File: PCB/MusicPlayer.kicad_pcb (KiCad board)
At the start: 4 copper layers, 96 x 96 mm, 79 parts, among them J1 3.7v LiPo, J2 USB_C_Receptacle_USB2.0_16P, J3 SSD1306D, J4 Conn_ST_STDC14, Q1 MMBT2907ALT1HTSA1, Q2 NMOS, SW1 ON_OFF, SW2 RESET, SW3 PLAY_PAUSE, SW4 NEXT, SW5 PREV, SW6 RotaryEncoder, U1 TPS61090, U2 LD1117S33TR_SOT223, U3 MCP73831T-2ACI/OT, U4 STM32G031K8Ux, U5 Music Maker FeatherWing, U6 MAX17048G, U7 USBLC6-2P6, U8 CH340C

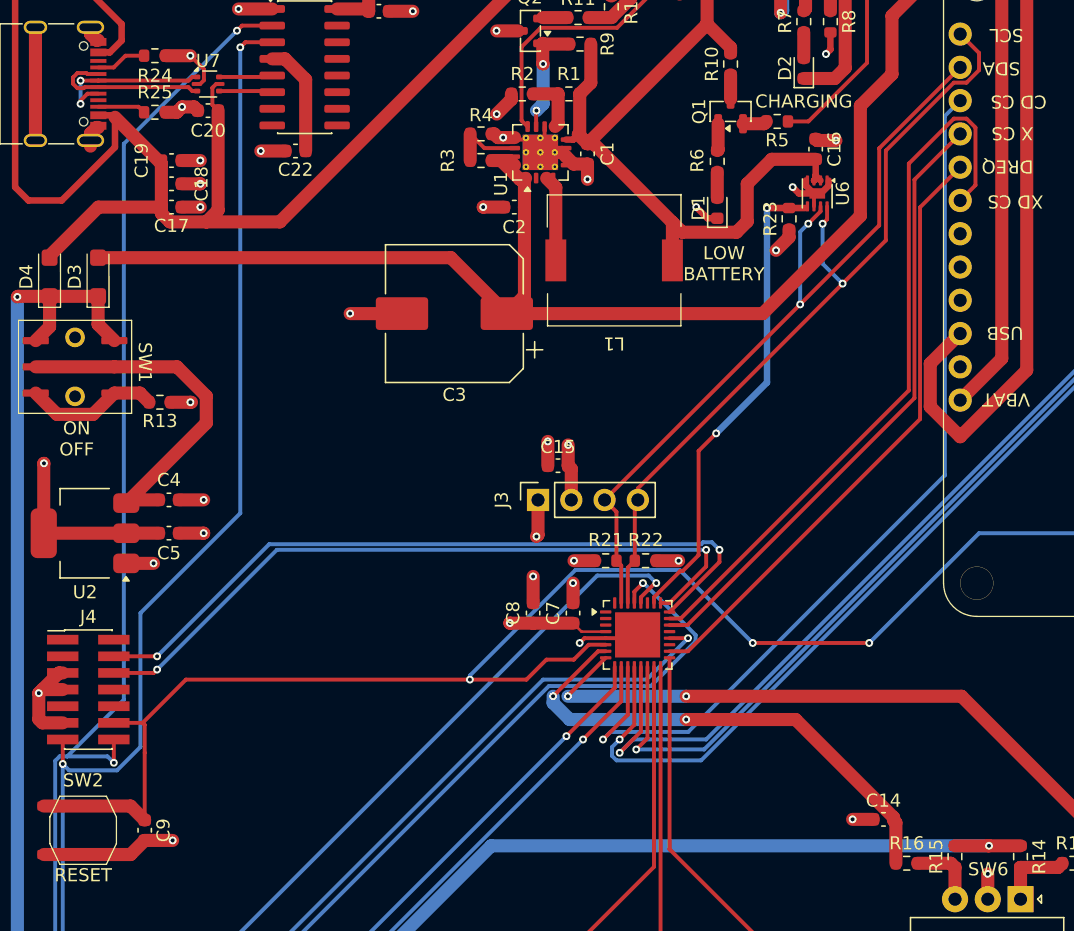
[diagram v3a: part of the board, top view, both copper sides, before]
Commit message: Finished making a PCB for it
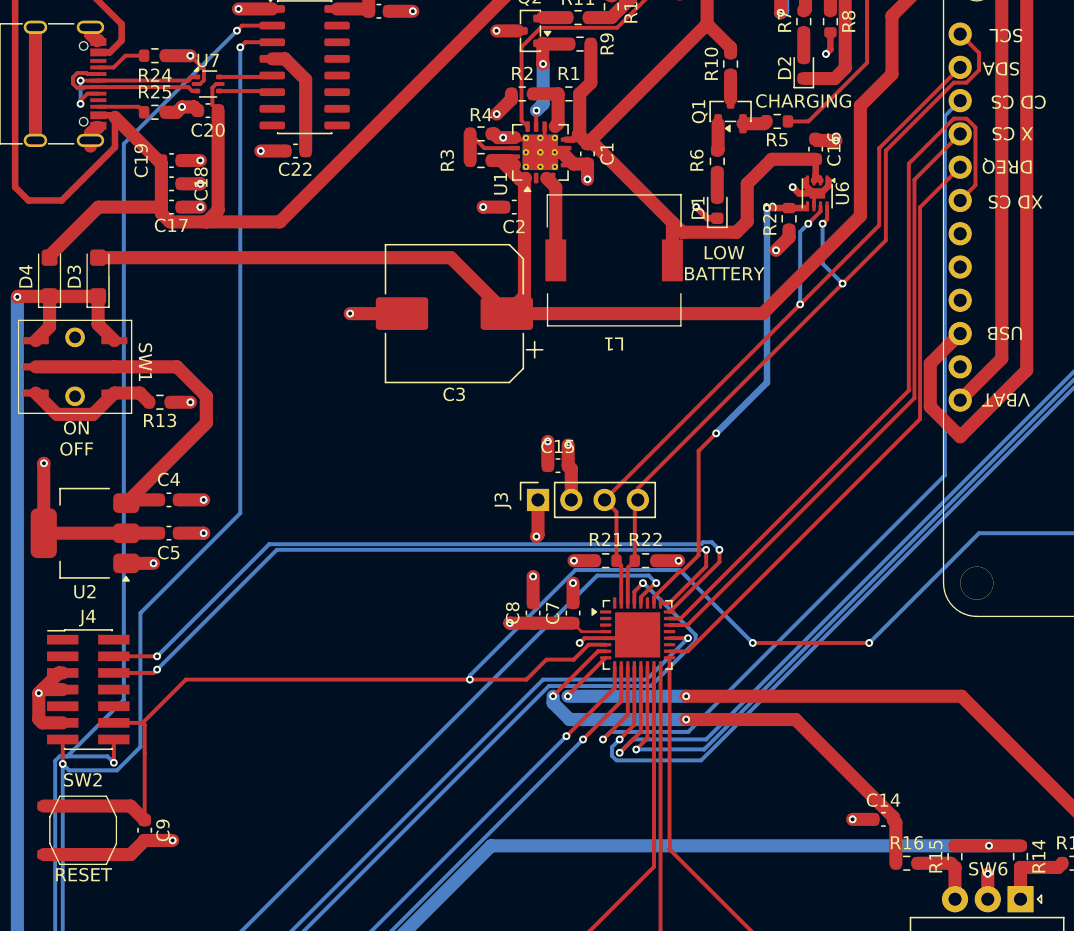
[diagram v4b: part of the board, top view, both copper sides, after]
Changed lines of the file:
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@@
 		(legacy_teardrops no)
 	)
-	(paper "A4")
+	(paper "USLetter")
+	(title_block
+		(title "Music Player")
+		(date "2026-02-02")
+		(rev "1")
+		(company "Joshua E")
+	)
 	(layers
 		(0 "F.Cu" signal)
@@
 			(outputformat 1)
 			(mirror no)
-			(drillshape 1)
+			(drillshape 0)
 			(scaleselection 1)
-			(outputdirectory "")
+			(outputdirectory "../../../../Downloads/")
 		)
 	)
@@
 	)
 	(segment
-		(start 119.634 87.543)
-		(end 119.721 87.543)
-		(width 1)
-		(layer "F.Cu")
-		(net 2)
-	)
-	(segment
 		(start 166.609 71.003194)
 		(end 166.609 70.616)
@@
 	)
 	(segment
-		(start 148.9635 104.2875)
-		(end 148.844 104.407)
-		(width 0.3)
-		(layer "F.Cu")
-		(net 5)
-	)
-	(segment
 		(start 114.742 97.54)
 		(end 108.442 97.54)
@@
 	)
 	(segment
-		(start 180.512 121.398)
+		(start 177.996 121.398)
 		(end 180.594 121.398)
 		(width 1)
@@
 	)
 	(segment
-		(start 177.996 121.398)
-		(end 180.512 121.398)
-		(width 1)
-		(layer "F.Cu")
-		(net 17)
-	)
-	(segment
 		(start 112.588 79.457)
 		(end 112.588 81.598)
@@
 	)
 	(segment
-		(start 111.256 62.988)
-		(end 111.252 62.992)
-		(width 0.3)
-		(layer "F.Cu")
-		(net 25)
-	)
-	(segment
 		(start 112.608 62.988)
 		(end 119.500704 62.988)
@@
 		(width 0.3)
 		(layer "F.Cu")
-		(net 57)
-	)
-	(segment
-		(start 145.375 66.22368)
-		(end 145.375 66.5055)
-		(width 0.3)
-		(layer "F.Cu")
